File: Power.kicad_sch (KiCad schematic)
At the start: 18 parts, among them U1 21700_DUAL_HOLDER, U2 TPS63070RNMR, U3 TPRT9013-33

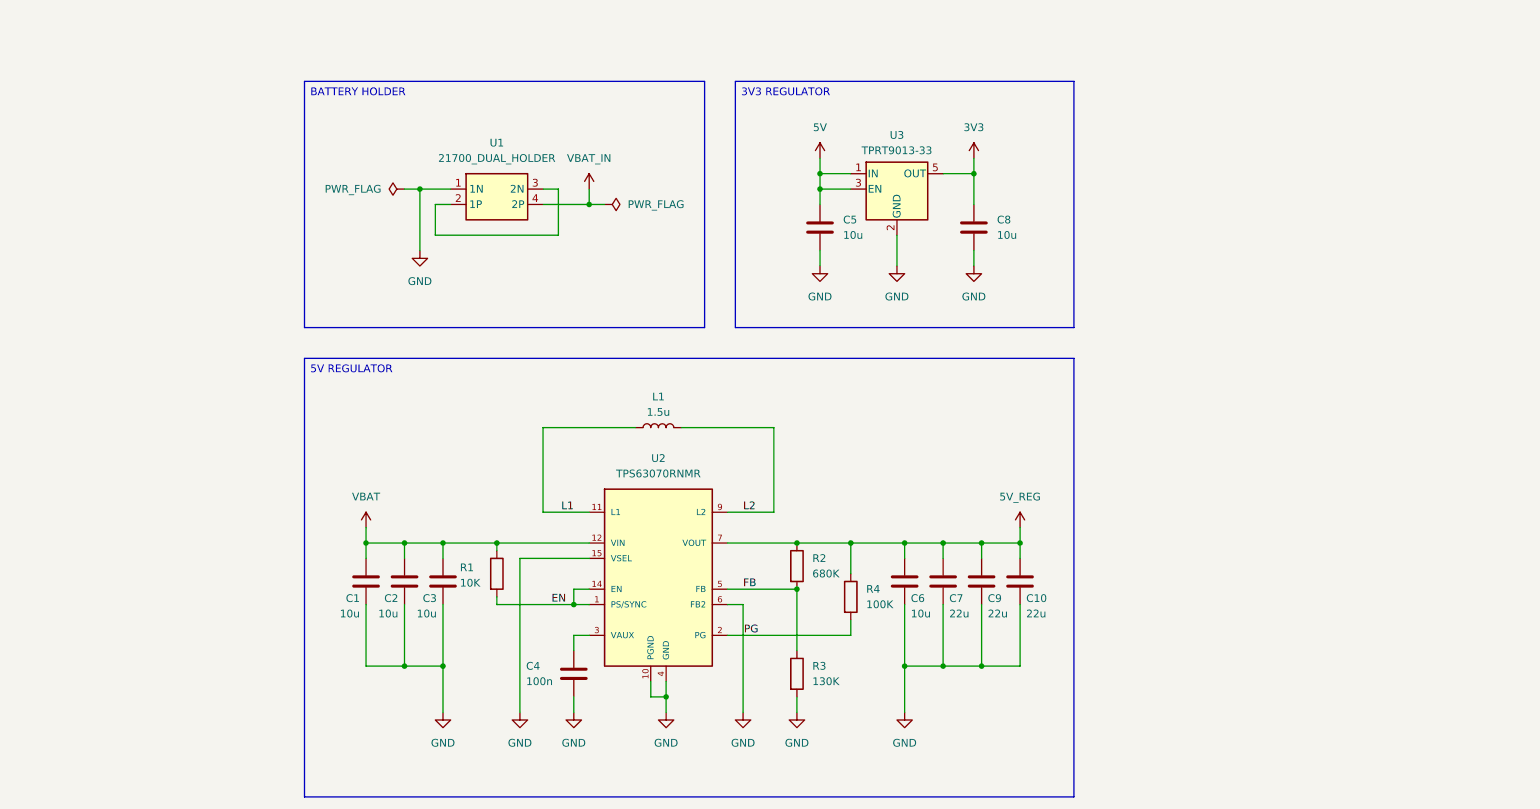
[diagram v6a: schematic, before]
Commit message: Connectors and tag
Added bulk capacitance for each ESC.
Added SWD connector.
Updated all tags.

TODO:
Add pads for the unconnected GPIO pins.
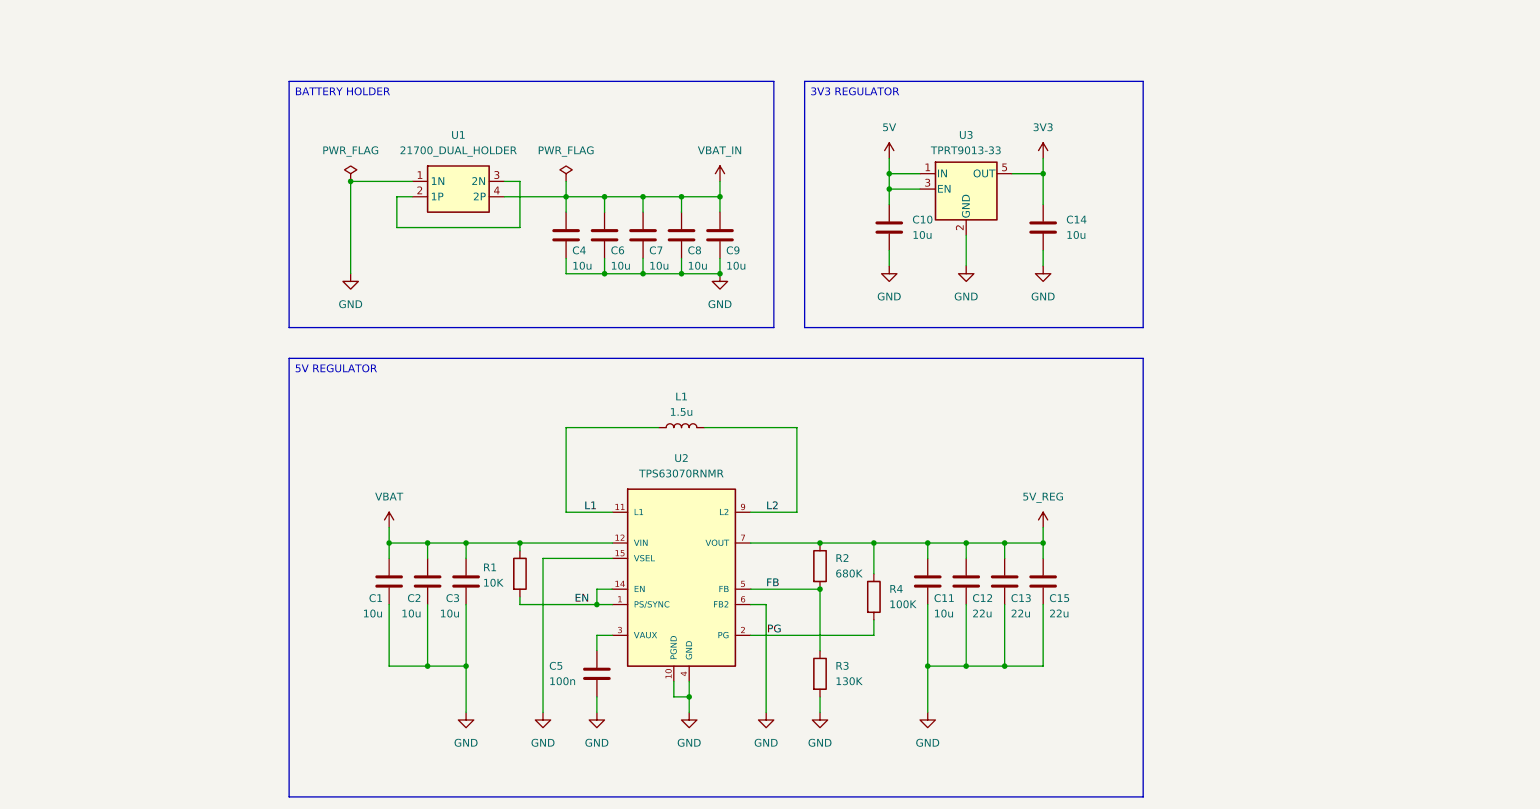
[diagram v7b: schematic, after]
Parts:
- added C4, C6, C7, C8, C9: 10u, symbol Device:C
- renumbered C5 to C10, C6 to C11, C7 to C12, C9 to C13, C8 to C14, C10 to C15, C4 to C5
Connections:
- net GND: now also C4.2, C6.2, C7.2, C8.2, C9.2
- net VBAT_IN: now also C4.1, C6.1, C7.1, C8.1, C9.1
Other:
- moved on the sheet: C1, C10, C11, C12, C13, C14, C15, C2, C3, C5, L1, R1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

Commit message: Missing labels and revision
First complete revision of the schematic.
Added missing labels.

TODO:
Continue reviewing the schematic.
Include net coloring.
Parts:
- C4, C6, C7, C8, C9: value 10u -> 22u; footprint (none) -> Capacitor_SMD:C_1206_3216Metric
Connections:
- net VAUX: now reaches C5.1, U2.3 (VAUX)
- net BAT_JUMP: now reaches U1.2 (1P), U1.3 (2N)
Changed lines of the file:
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@@
 	)
 	(label "FB"
-		(at 148.59 118.11 0)
+		(at 151.13 118.11 0)
 		(effects
 			(font
@@
 	)
 	(label "PG"
-		(at 151.13 125.73 180)
+		(at 151.13 125.73 0)
 		(effects
 			(font
 				(size 1.27 1.27)
 			)
-			(justify right bottom)
+			(justify left bottom)
 		)
 	)
@@
 		)
 	)
+	(label "BAT_JUMP"
+		(at 92.71 58.42 0)
+		(effects
+			(font
+				(size 1.27 1.27)
+			)
+			(justify left bottom)
+		)
+	)
+	(label "VAUX"
+		(at 123.19 125.73 180)
+		(effects
+			(font
+				(size 1.27 1.27)
+			)
+			(justify right bottom)
+		)
+	)
 	(label "EN"
 		(at 119.38 120.65 180)
@@
 			)
 		)
-		(property "Value" "10u"
+		(property "Value" "22u"
 			(at 135.636 64.77 0)
 			(effects
@@
 			)
 		)
-		(property "Footprint" ""
+		(property "Footprint" "Capacitor_SMD:C_1206_3216Metric"
 			(at 135.5852 63.5 0)
 			(effects
@@
 			)
 		)
-		(property "Value" "10u"
+		(property "Value" "22u"
 			(at 122.936 64.77 0)
 			(effects
@@
 			)
 		)
-		(property "Footprint" ""
+		(property "Footprint" "Capacitor_SMD:C_1206_3216Metric"
 			(at 122.8852 63.5 0)
 			(effects
@@
 			)
 		)
-		(property "Value" "10u"
+		(property "Value" "22u"
 			(at 116.586 64.77 0)
 			(effects
@@
 			)
 		)
-		(property "Footprint" ""
+		(property "Footprint" "Capacitor_SMD:C_1206_3216Metric"
 			(at 116.5352 63.5 0)
 			(effects
@@
 			)
 		)
-		(property "Value" "10u"
+		(property "Value" "22u"
 			(at 129.286 64.77 0)
 			(effects
@@
 			)
 		)
-		(property "Footprint" ""
+		(property "Footprint" "Capacitor_SMD:C_1206_3216Metric"
 			(at 129.2352 63.5 0)
 			(effects
@@
 			)
 		)
-		(property "Value" "10u"
+		(property "Value" "22u"
 			(at 141.986 64.77 0)
 			(effects
@@
 			)
 		)
-		(property "Footprint" ""
+		(property "Footprint" "Capacitor_SMD:C_1206_3216Metric"
 			(at 141.9352 63.5 0)
 			(effects
